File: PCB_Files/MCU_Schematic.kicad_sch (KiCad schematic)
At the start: 36 parts, among them J10 2D_LiDAR, J2 Ultrasonic_Sensor, J3 OLED_Display, J5 USB_C_Receptacle_USB2.0_16P, J6 Conn_01x04_Pin, J9 IMU, SW1 SW_SPDT, U1 STM32F411RETx, Y1 16MHz

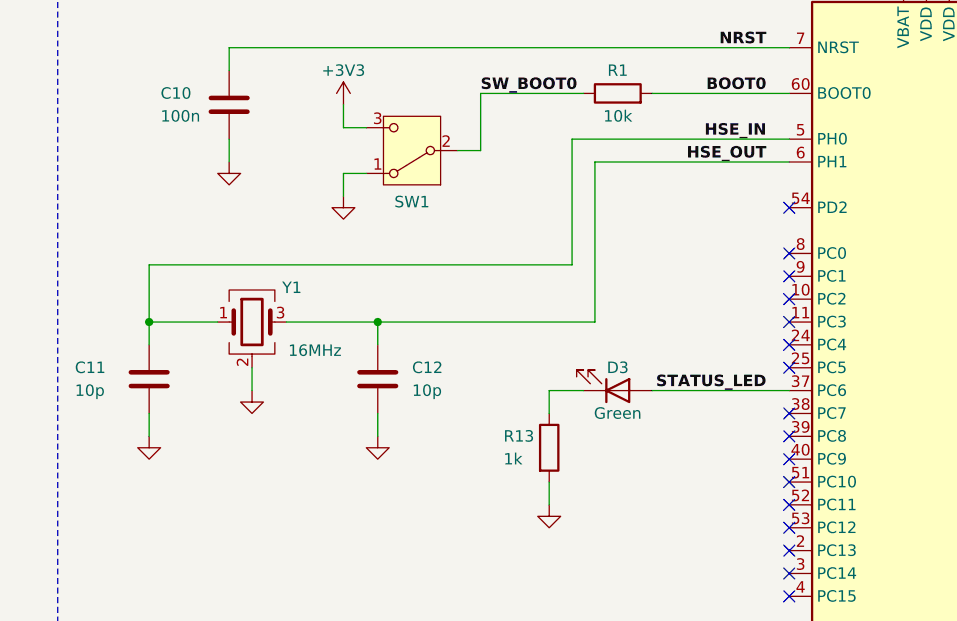
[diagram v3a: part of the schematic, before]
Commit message: Added MOT_STBY output from MCU pin 24 to enable low-power sleep state on motor controllers.
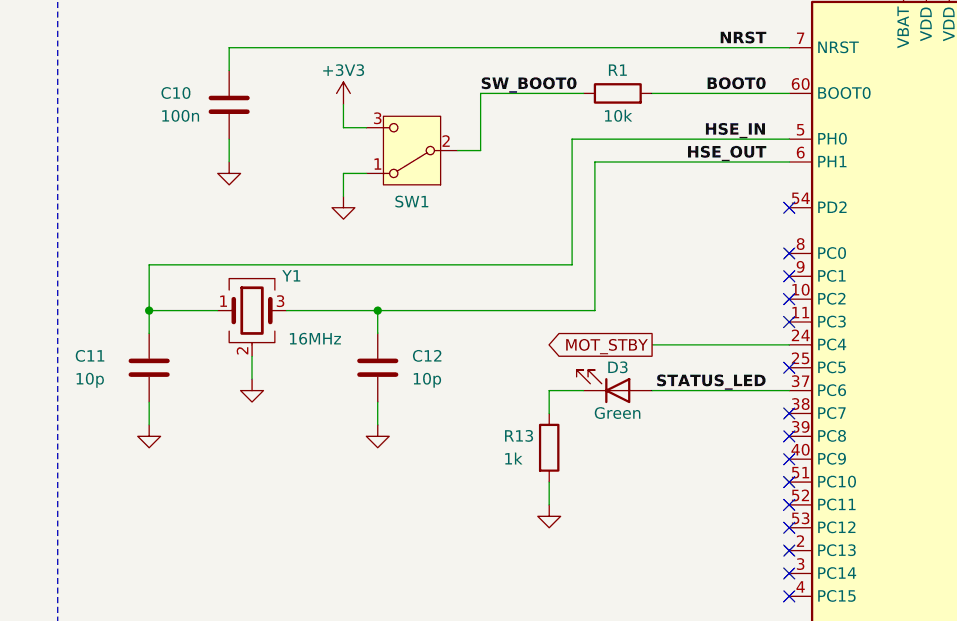
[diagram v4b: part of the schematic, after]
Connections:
- net MOT_STBY: now reaches U1.24 (PC4)
- no-connect marks 29 -> 28
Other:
- moved on the sheet: C11, C12, Y1
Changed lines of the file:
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@@
 	)
 	(junction
-		(at 53.34 124.46)
+		(at 27.94 123.19)
 		(diameter 0)
 		(color 0 0 0 0)
@@
 	)
 	(junction
-		(at 27.94 124.46)
-		(diameter 0)
-		(color 0 0 0 0)
-	)
-	(junction
 		(at 35.56 39.37)
 		(diameter 0)
@@
 	)
 	(junction
+		(at 53.34 123.19)
+		(diameter 0)
+		(color 0 0 0 0)
+	)
+	(junction
 		(at 64.77 39.37)
 		(diameter 0)
@@
 	)
 	(no_connect
-		(at 99.06 127)
-	)
-	(no_connect
 		(at 99.06 116.84)
 	)
@@
 	(wire
 		(pts
-			(xy 53.34 124.46) (xy 53.34 127)
-		)
-		(stroke
-			(width 0)
-			(type default)
-		)
-	)
-	(wire
-		(pts
 			(xy 212.09 149.86) (xy 210.82 149.86)
 		)
@@
 	(wire
 		(pts
-			(xy 39.37 129.54) (xy 39.37 132.08)
+			(xy 39.37 128.27) (xy 39.37 130.81)
 		)
 		(stroke
@@
 	(wire
 		(pts
-			(xy 35.56 124.46) (xy 27.94 124.46)
+			(xy 35.56 123.19) (xy 27.94 123.19)
 		)
 		(stroke
@@
 	(wire
 		(pts
-			(xy 27.94 134.62) (xy 27.94 137.16)
+			(xy 27.94 133.35) (xy 27.94 135.89)
 		)
 		(stroke
@@
 	(wire
 		(pts
+			(xy 27.94 123.19) (xy 27.94 118.11)
+		)
+		(stroke
+			(width 0)
+			(type default)
+		)
+	)
+	(wire
+		(pts
 			(xy 35.56 26.67) (xy 35.56 29.21)
 		)
@@
 	(wire
 		(pts
+			(xy 27.94 123.19) (xy 27.94 125.73)
+		)
+		(stroke
+			(width 0)
+			(type default)
+		)
+	)
+	(wire
+		(pts
 			(xy 134.62 160.02) (xy 148.59 160.02)
 		)
@@
 	(wire
 		(pts
-			(xy 43.18 124.46) (xy 53.34 124.46)
+			(xy 43.18 123.19) (xy 53.34 123.19)
 		)
 		(stroke
@@
 	(wire
 		(pts
-			(xy 27.94 124.46) (xy 27.94 118.11)
-		)
-		(stroke
-			(width 0)
-			(type default)
-		)
-	)
-	(wire
-		(pts
 			(xy 226.06 109.22) (xy 228.6 109.22)
 		)
@@
 	(wire
 		(pts
+			(xy 83.82 127) (xy 99.06 127)
+		)
+		(stroke
+			(width 0)
+			(type default)
+		)
+	)
+	(wire
+		(pts
 			(xy 116.84 85.09) (xy 114.3 85.09)
 		)
@@
 	(wire
 		(pts
+			(xy 53.34 123.19) (xy 53.34 125.73)
+		)
+		(stroke
+			(width 0)
+			(type default)
+		)
+	)
+	(wire
+		(pts
 			(xy 134.62 142.24) (xy 148.59 142.24)
 		)
@@
 	(wire
 		(pts
-			(xy 53.34 124.46) (xy 77.47 124.46)
+			(xy 53.34 123.19) (xy 77.47 123.19)
 		)
 		(stroke
@@
 	(wire
 		(pts
-			(xy 53.34 134.62) (xy 53.34 137.16)
+			(xy 53.34 133.35) (xy 53.34 135.89)
 		)
 		(stroke
@@
 	(wire
 		(pts
-			(xy 27.94 124.46) (xy 27.94 127)
-		)
-		(stroke
-			(width 0)
-			(type default)
-		)
-	)
-	(wire
-		(pts
 			(xy 130.81 26.67) (xy 124.46 26.67)
 		)
@@
 	(wire
 		(pts
-			(xy 77.47 106.68) (xy 77.47 124.46)
+			(xy 77.47 106.68) (xy 77.47 123.19)
 		)
 		(stroke
@@
 		)
 	)
+	(global_label "MOT_STBY"
+		(shape output)
+		(at 83.82 127 180)
+		(fields_autoplaced yes)
+		(effects
+			(font
+				(size 1.27 1.27)
+			)
+			(justify right)
+		)
+		(property "Intersheetrefs" "${INTERSHEET_REFS}"
+			(at 71.582 127 0)
+			(hide yes)
+			(show_name no)
+			(do_not_autoplace no)
+			(effects
+				(font
+					(size 1.27 1.27)
+				)
+				(justify right)
+			)
+		)
+	)
 	(global_label "MOT2_PWM"
 		(shape output)
@@
 	(symbol
 		(lib_id "Device:C")
-		(at 27.94 130.81 0)
+		(at 27.94 129.54 0)
 		(unit 1)
 		(body_style 1)
@@
 		(dnp no)
 		(property "Reference" "C11"
-			(at 19.685 129.54 0)
+			(at 19.685 128.27 0)
 			(show_name no)
 			(do_not_autoplace no)
@@
 		)
 		(property "Value" "10p"
-			(at 19.685 132.08 0)
+			(at 19.685 130.81 0)
 			(show_name no)
 			(do_not_autoplace no)
@@
 		)
 		(property "Footprint" "Capacitor_SMD:C_0603_1608Metric"
-			(at 28.9052 134.62 0)
+			(at 28.9052 133.35 0)
 			(hide yes)
 			(show_name no)
@@
 		)
 		(property "Datasheet" ""
-			(at 27.94 130.81 0)
+			(at 27.94 129.54 0)
 			(hide yes)
 			(show_name no)
@@
 		)
 		(property "Description" "Unpolarized capacitor"
-			(at 27.94 130.81 0)
+			(at 27.94 129.54 0)
 			(hide yes)
 			(show_name no)
@@
 	(symbol
 		(lib_id "Device:Crystal_GND24")
-		(at 39.37 124.46 0)
+		(at 39.37 123.19 0)
 		(unit 1)
 		(body_style 1)
@@
 		(dnp no)
 		(property "Reference" "Y1"
-			(at 43.815 120.65 0)
+			(at 43.815 119.38 0)
 			(show_name no)
 			(do_not_autoplace no)
@@
 		)
 		(property "Value" "16MHz"
-			(at 46.355 127.635 0)
+			(at 46.355 126.365 0)
 			(show_name no)
 			(do_not_autoplace no)
@@
 		)
 		(property "Footprint" ""
-			(at 39.37 124.46 0)
+			(at 39.37 123.19 0)
 			(hide yes)
 			(show_name no)
@@
 		)
 		(property "Datasheet" ""
-			(at 39.37 124.46 0)
+			(at 39.37 123.19 0)
 			(hide yes)
 			(show_name no)
@@
 		)
 		(property "Description" "Four pin crystal, GND on pins 2 and 4"
-			(at 39.37 124.46 0)
+			(at 39.37 123.19 0)
 			(hide yes)
 			(show_name no)
@@
 		)
 		(property private "KLC_S3.3" "The rectangle is not a symbol body but a graphical element"
-			(at 39.37 137.16 0)
+			(at 39.37 135.89 0)
 			(hide yes)
 			(show_name yes)
@@
 		)
 		(property private "KLC_S4.1" "Some pins are on 50mil grid to make the symbol small"
-			(at 39.37 139.7 0)
+			(at 39.37 138.43 0)
 			(hide yes)
 			(show_name yes)
@@
 	(symbol
 		(lib_id "Device:C")
-		(at 53.34 130.81 0)
+		(at 53.34 129.54 0)
 		(unit 1)
 		(body_style 1)
@@
 		(fields_autoplaced yes)
 		(property "Reference" "C12"
-			(at 57.15 129.5399 0)
+			(at 57.15 128.2699 0)
 			(show_name no)
 			(do_not_autoplace no)
@@
 		)
 		(property "Value" "10p"
-			(at 57.15 132.0799 0)
+			(at 57.15 130.8099 0)
 			(show_name no)
 			(do_not_autoplace no)
@@
 		)
 		(property "Footprint" "Capacitor_SMD:C_0603_1608Metric"
-			(at 54.3052 134.62 0)
+			(at 54.3052 133.35 0)
 			(hide yes)
 			(show_name no)
@@
 		)
 		(property "Datasheet" ""
-			(at 53.34 130.81 0)
+			(at 53.34 129.54 0)
 			(hide yes)
 			(show_name no)
@@
 		)
 		(property "Description" "Unpolarized capacitor"
-			(at 53.34 130.81 0)
+			(at 53.34 129.54 0)
 			(hide yes)
 			(show_name no)
@@
 	(symbol
 		(lib_id "power:GND")
-		(at 53.34 137.16 0)
+		(at 53.34 135.89 0)
 		(unit 1)
 		(body_style 1)
@@
 		(fields_autoplaced yes)
 		(property "Reference" "#PWR013"
-			(at 53.34 143.51 0)
+			(at 53.34 142.24 0)
 			(hide yes)
 			(show_name no)
@@
 		)
 		(property "Value" "GND"
-			(at 53.34 142.24 0)
+			(at 53.34 140.97 0)
 			(hide yes)
 			(show_name no)
@@
 		)
 		(property "Footprint" ""
-			(at 53.34 137.16 0)
+			(at 53.34 135.89 0)
 			(hide yes)
 			(show_name no)
@@
 		)
 		(property "Datasheet" ""
-			(at 53.34 137.16 0)
+			(at 53.34 135.89 0)
 			(hide yes)
 			(show_name no)
@@
 		)
 		(property "Description" "Power symbol creates a global label with name \"GND\" , ground"
-			(at 53.34 137.16 0)
+			(at 53.34 135.89 0)
 			(hide yes)
 			(show_name no)
@@
 	(symbol
 		(lib_id "power:GND")
-		(at 39.37 132.08 0)
+		(at 39.37 130.81 0)
 		(unit 1)
 		(body_style 1)
@@
 		(fields_autoplaced yes)
 		(property "Reference" "#PWR010"
-			(at 39.37 138.43 0)
+			(at 39.37 137.16 0)
 			(hide yes)
 			(show_name no)
@@
 		)
 		(property "Value" "GND"
-			(at 39.37 137.16 0)
+			(at 39.37 135.89 0)
 			(hide yes)
 			(show_name no)
@@
 		)
 		(property "Footprint" ""
-			(at 39.37 132.08 0)
+			(at 39.37 130.81 0)
 			(hide yes)
 			(show_name no)
@@
 		)
 		(property "Datasheet" ""
-			(at 39.37 132.08 0)
+			(at 39.37 130.81 0)
 			(hide yes)
 			(show_name no)
@@
 		)
 		(property "Description" "Power symbol creates a global label with name \"GND\" , ground"
-			(at 39.37 132.08 0)
+			(at 39.37 130.81 0)
 			(hide yes)
 			(show_name no)
@@
 	(symbol
 		(lib_id "power:GND")
-		(at 27.94 137.16 0)
+		(at 27.94 135.89 0)
 		(unit 1)
 		(body_style 1)
@@
 		(fields_autoplaced yes)
 		(property "Reference" "#PWR012"
-			(at 27.94 143.51 0)
+			(at 27.94 142.24 0)
 			(hide yes)
 			(show_name no)
@@
 		)
 		(property "Value" "GND"
-			(at 27.94 142.24 0)
+			(at 27.94 140.97 0)
 			(hide yes)
 			(show_name no)
@@
 		)
 		(property "Footprint" ""
-			(at 27.94 137.16 0)
+			(at 27.94 135.89 0)
 			(hide yes)
 			(show_name no)
@@
 		)
 		(property "Datasheet" ""
-			(at 27.94 137.16 0)
+			(at 27.94 135.89 0)
 			(hide yes)
 			(show_name no)
@@
 		)
 		(property "Description" "Power symbol creates a global label with name \"GND\" , ground"
-			(at 27.94 137.16 0)
+			(at 27.94 135.89 0)
 			(hide yes)
 			(show_name no)

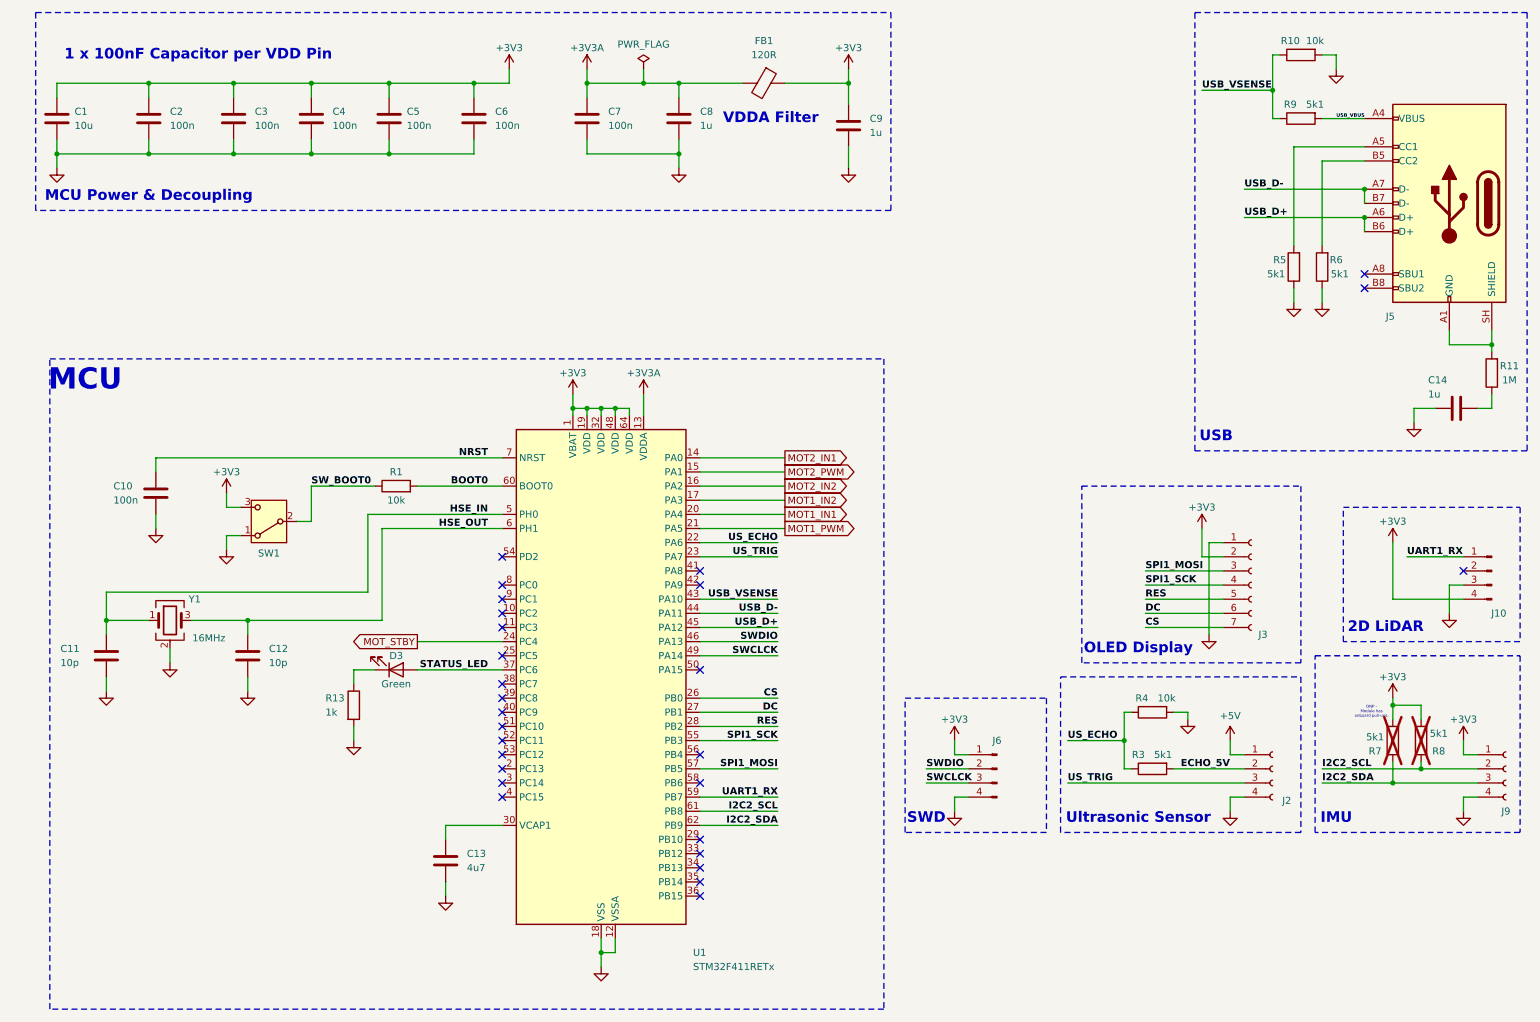
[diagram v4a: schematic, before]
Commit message: Changed +BATT net name to +VBAT, +BATT_SW to +VBAT_SW, and now motor controllers are powered by net name +VBAT_SW. This clearly seperates +VBAT before the switch, +VBAT_SW after the switch, +5V, and +3V3 / +3V3A.
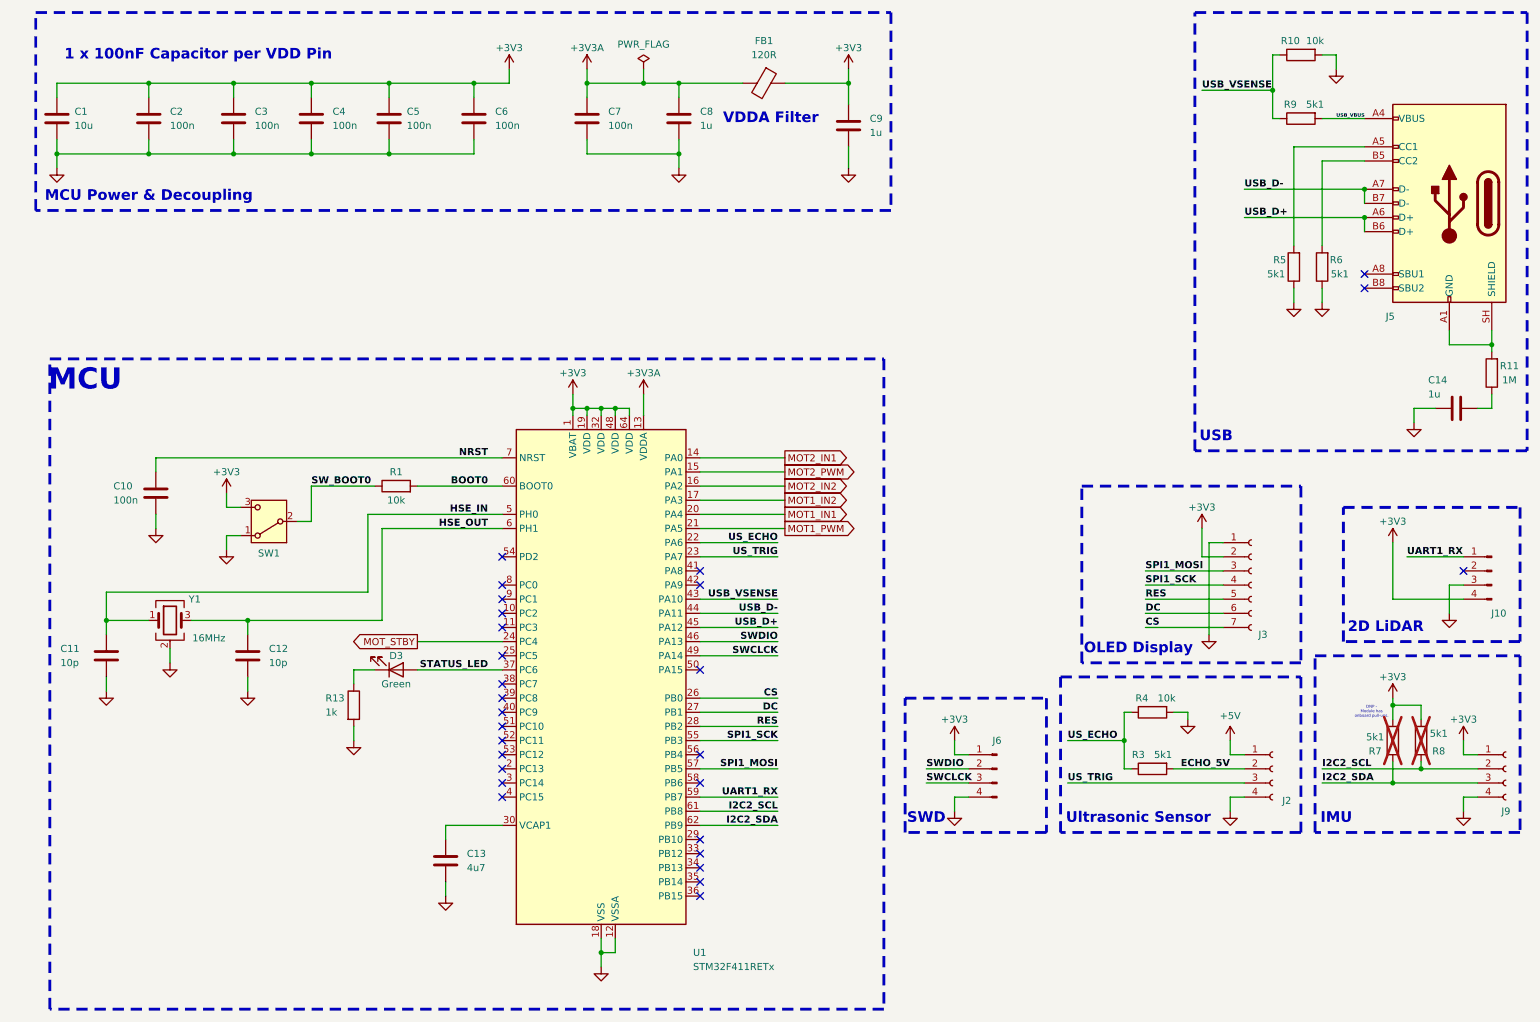
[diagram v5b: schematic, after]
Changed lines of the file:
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@@
 		(end 242.57 161.29)
 		(stroke
-			(width 0.127)
+			(width 0.508)
 			(type dash)
 		)
@@
 		(end 283.21 92.71)
 		(stroke
-			(width 0.127)
+			(width 0.508)
 			(type dash)
 		)
@@
 		(end 242.57 130.81)
 		(stroke
-			(width 0.127)
+			(width 0.508)
 			(type dash)
 		)
@@
 		(end 281.94 127)
 		(stroke
-			(width 0.127)
+			(width 0.508)
 			(type dash)
 		)
@@
 		(end 168.91 49.53)
 		(stroke
-			(width 0.127)
+			(width 0.508)
 			(type dash)
 		)
@@
 		(end 281.94 161.29)
 		(stroke
-			(width 0.127)
+			(width 0.508)
 			(type dash)
 		)
@@
 		(end 167.64 193.04)
 		(stroke
-			(width 0.127)
+			(width 0.508)
 			(type dash)
 		)
@@
 		(end 196.85 161.29)
 		(stroke
-			(width 0.127)
+			(width 0.508)
 			(type dash)
 		)
